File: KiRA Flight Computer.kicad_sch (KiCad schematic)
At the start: 44 parts, among them J1 Conn_01x04_Pin, J2 USB_C_Receptacle_USB2.0_14P, SW1 SW_Push, SW2 SW_SPDT, U1 ICM-426788P, U2 STM32F407VGTx, U3 MMC5883MA, U4 DPS368, U6 Wio-SX1262, U7 USBLC6-2P6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

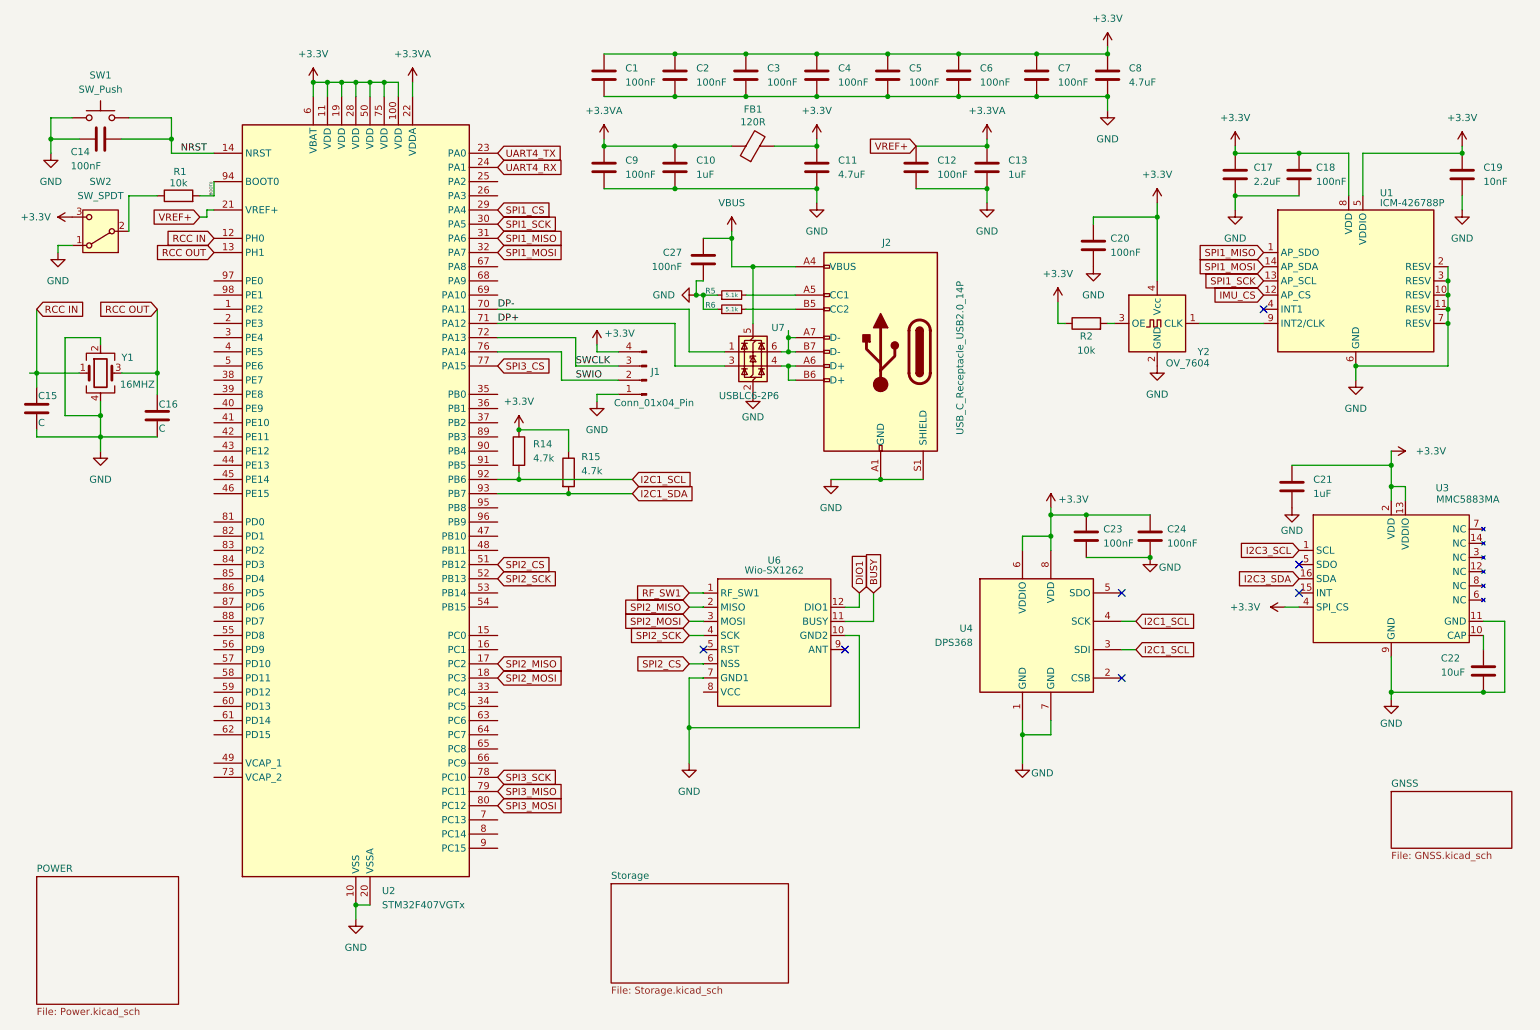
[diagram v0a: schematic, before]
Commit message: add sd card reader
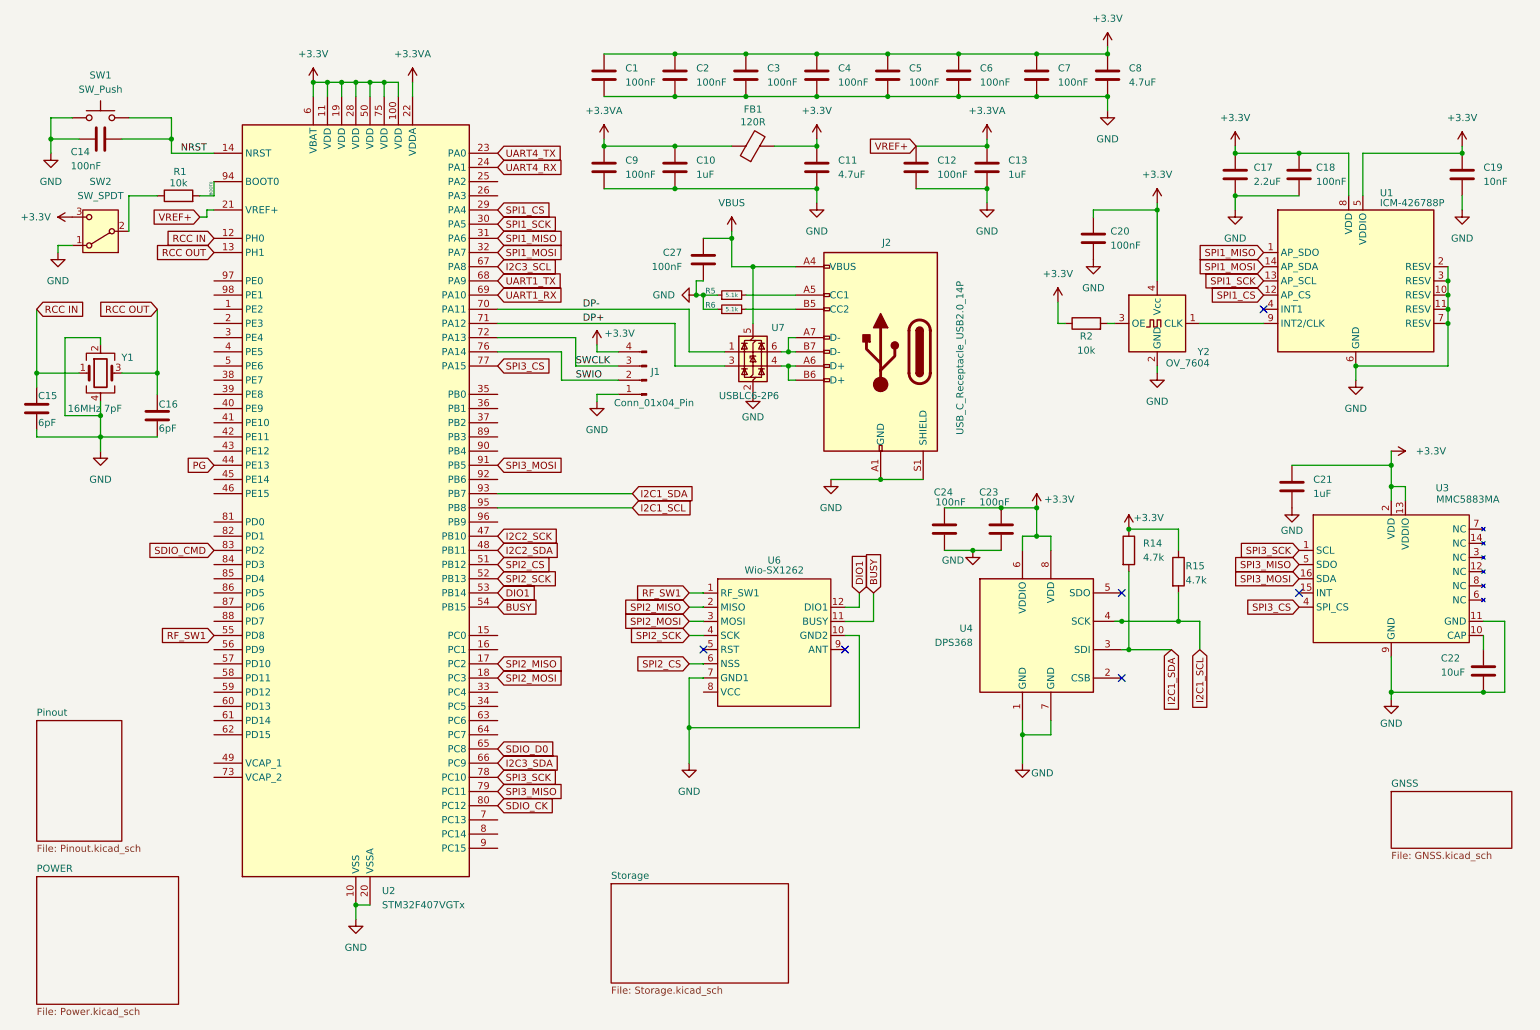
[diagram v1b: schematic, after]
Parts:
- C15, C16: value C -> 6pF
- Y1: value 16MHZ -> 16MHz 7pF
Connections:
- net IMU_CS is gone; now on net SPI1_CS: U1.12 (AP_CS)
- net +3.3V: no longer U3.4 (SPI_CS)
- net BUSY: now also U2.54 (PB15)
- net DIO1: now also U2.53 (PB14)
- net I2C1_SCL: now also R15.2, U2.95 (PB8); no longer R14.2, U2.92 (PB6), U4.3 (SDI)
- net I2C1_SDA: now also R14.2, U4.3 (SDI); no longer R15.2
- net I2C3_SCL: now also U2.67 (PA8); no longer U3.1 (SCL)
- net I2C3_SDA: now also U2.66 (PC9); no longer U3.16 (SDA)
- net RF_SW1: now also U2.55 (PD8)
- net SPI3_CS: now also U3.4 (SPI_CS)
- net SPI3_MISO: now also U3.5 (SDO)
- net SPI3_MOSI: now also U2.91 (PB5), U3.16 (SDA); no longer U2.80 (PC12)
- net SPI3_SCK: now also U3.1 (SCL)
- net PG: now reaches U2.44 (PE13)
- net I2C2_SCK: now reaches U2.47 (PB10)
- net I2C2_SDA: now reaches U2.48 (PB11)
- net SDIO_D0: now reaches U2.65 (PC8)
- net UART1_TX: now reaches U2.68 (PA9)
- net UART1_RX: now reaches U2.69 (PA10)
- net SDIO_CMD: now reaches U2.83 (PD2)
- new net SDIO_CK: U2.80 (PC12)
- no-connect marks 7 -> 6
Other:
- added sheet Pinout (Pinout.kicad_sch)
- moved on the sheet: C20, C23, C24, R14, R15

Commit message: "Update KiRA Flight Computer schematic and PCB files"
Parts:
- C1, C10, C11, C12, C13, C14, C15, C16, C17, C18, C2, C20, C21, C23, C24, C3, C4, C5, C6, C7, C8, C9: footprint (none) -> Capacitor_SMD:C_0603_1608Metric
- C19: footprint (none) -> Capacitor_SMD:C_0402_1005Metric
- C22: footprint (none) -> Capacitor_SMD:C_1206_3216Metric
- C27: footprint (none) -> Capacitor_SMD:C_0402_1005Metric_Pad0.74x0.62mm_HandSolder
- FB1: footprint (none) -> Inductor_SMD:L_1206_3216Metric
- J1: footprint (none) -> Connector_PinHeader_2.54mm:PinHeader_1x04_P2.54mm_Vertical
- J2: footprint (none) -> Connector_USB:USB_C_Receptacle_GCT_USB4105-xx-A_16P_TopMnt_Horizontal
- R1, R2: footprint (none) -> Resistor_SMD:R_0402_1005Metric
- R14, R15, R5, R6: footprint (none) -> Resistor_SMD:R_0603_1608Metric
- SW1: footprint (none) -> Button_Switch_SMD:SW_Push_1P1T_NO_CK_PTS125Sx43PSMTR
- SW2: footprint (none) -> Button_Switch_SMD:SW_SPDT_CK_JS102011SAQN
- U6: footprint ProLib_pcs_2024-10-14:Module:MODULE12P-1.27-11X11.6MM -> dep:WIO SX1262
- Y1: footprint (none) -> Crystal:Crystal_SMD_3225-4Pin_3.2x2.5mm
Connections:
- net +3.3V: now also U6.8 (VCC)
- net DP+: now also U7.1 (I/O1); no longer U7.3 (I/O2)
- net DP-: now also U7.3 (I/O2); no longer U7.1 (I/O1)
- net at J2.A6 (D+), J2.B6 (D+): now also U7.6 (I/O1); no longer U7.4 (I/O2)
- net at J2.A7 (D-), J2.B7 (D-): now also U7.4 (I/O2); no longer U7.6 (I/O1)
- net UART2_TX: now reaches U2.25 (PA2)
- net UART2_RX: now reaches U2.26 (PA3)
- net BUZZER: now reaches U2.56 (PD9)
- net MPU_CLK: now reaches U1.9 (INT2/CLK), Y2.1 (CLK)
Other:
- moved on the sheet: R5, R6, U7

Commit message: Update PCB
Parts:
- SW1: footprint Button_Switch_SMD:SW_Push_1P1T_NO_CK_PTS125Sx43PSMTR -> Button_Switch_SMD:SW_Push_1P1T_NO_CK_KSC6xxJ
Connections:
- net +3.3V: now also J1.1 (Pin_1); no longer J1.4 (Pin_4)
- net GND: now also J1.4 (Pin_4); no longer J1.1 (Pin_1)
- net SWCLK: now also J1.2 (Pin_2); no longer J1.3 (Pin_3)
- net SWIO: now also J1.3 (Pin_3); no longer J1.2 (Pin_2)
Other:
- moved on the sheet: J1
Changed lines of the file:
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@@
 	(paper "A4")
 	(junction
-		(at 135.89 63.5)
+		(at 217.17 48.26)
 		(diameter 0)
 		(color 0 0 0 0)
 	)
 	(junction
-		(at 217.17 48.26)
+		(at 135.89 63.5)
 		(diameter 0)
 		(color 0 0 0 0)
@@
 	)
 	(junction
+		(at 146.05 63.5)
+		(diameter 0)
+		(color 0 0 0 0)
+	)
+	(junction
 		(at 143.51 27.94)
 		(diameter 0)
@@
 	)
 	(junction
-		(at 134.62 63.5)
-		(diameter 0)
-		(color 0 0 0 0)
-	)
-	(junction
 		(at 16.51 77.47)
 		(diameter 0)
@@
 	)
 	(junction
-		(at 142.24 58.42)
-		(diameter 0)
-		(color 0 0 0 0)
-	)
-	(junction
 		(at 212.09 105.41)
 		(diameter 0)
@@
 	(wire
 		(pts
-			(xy 142.24 81.28) (xy 144.78 81.28)
-		)
-		(stroke
-			(width 0)
-			(type default)
-		)
-	)
-	(wire
-		(pts
 			(xy 156.21 20.32) (xy 168.91 20.32)
 		)
@@
 	(wire
 		(pts
-			(xy 135.89 66.04) (xy 135.89 63.5)
+			(xy 146.05 66.04) (xy 146.05 63.5)
 		)
 		(stroke
@@
 	(wire
 		(pts
-			(xy 146.05 66.04) (xy 135.89 66.04)
-		)
-		(stroke
-			(width 0)
-			(type default)
-		)
-	)
-	(wire
-		(pts
 			(xy 195.58 101.6) (xy 195.58 106.68)
 		)
@@
 	(wire
 		(pts
-			(xy 134.62 63.5) (xy 135.89 63.5)
-		)
-		(stroke
-			(width 0)
-			(type default)
-		)
-	)
-	(wire
-		(pts
 			(xy 259.08 128.27) (xy 259.08 134.62)
 		)
@@
 	(wire
 		(pts
+			(xy 135.89 63.5) (xy 146.05 63.5)
+		)
+		(stroke
+			(width 0)
+			(type default)
+		)
+	)
+	(wire
+		(pts
 			(xy 78.74 25.4) (xy 78.74 27.94)
 		)
@@
 	(wire
 		(pts
-			(xy 135.89 60.96) (xy 134.62 60.96)
-		)
-		(stroke
-			(width 0)
-			(type default)
-		)
-	)
-	(wire
-		(pts
-			(xy 142.24 58.42) (xy 152.4 58.42)
-		)
-		(stroke
-			(width 0)
-			(type default)
-		)
-	)
-	(wire
-		(pts
 			(xy 99.06 68.58) (xy 130.81 68.58)
 		)
@@
 	(wire
 		(pts
-			(xy 140.97 58.42) (xy 142.24 58.42)
+			(xy 140.97 58.42) (xy 152.4 58.42)
 		)
 		(stroke
@@
 	(wire
 		(pts
-			(xy 193.04 109.22) (xy 193.04 106.68)
+			(xy 135.89 63.5) (xy 134.62 63.5)
 		)
 		(stroke
@@
 	(wire
 		(pts
-			(xy 135.89 132.08) (xy 133.35 132.08)
+			(xy 193.04 109.22) (xy 193.04 106.68)
 		)
 		(stroke
@@
 	(wire
 		(pts
-			(xy 19.05 35.56) (xy 19.05 38.1)
+			(xy 135.89 132.08) (xy 133.35 132.08)
 		)
 		(stroke
@@
 	(wire
 		(pts
-			(xy 21.59 71.12) (xy 21.59 85.09)
+			(xy 19.05 35.56) (xy 19.05 38.1)
 		)
 		(stroke
@@
 	(wire
 		(pts
-			(xy 130.81 20.32) (xy 143.51 20.32)
+			(xy 21.59 71.12) (xy 21.59 85.09)
 		)
 		(stroke
@@
 	(wire
 		(pts
-			(xy 38.1 77.47) (xy 31.75 77.47)
+			(xy 130.81 20.32) (xy 143.51 20.32)
 		)
 		(stroke
@@
 	(wire
 		(pts
-			(xy 156.21 35.56) (xy 156.21 36.83)
+			(xy 38.1 77.47) (xy 31.75 77.47)
 		)
 		(stroke
@@
 	(wire
 		(pts
-			(xy 219.71 127) (xy 212.09 127)
+			(xy 156.21 35.56) (xy 156.21 36.83)
 		)
 		(stroke
@@
 	(wire
 		(pts
-			(xy 135.89 63.5) (xy 146.05 63.5)
+			(xy 219.71 127) (xy 212.09 127)
 		)
 		(stroke
@@
 	(wire
 		(pts
-			(xy 142.24 58.42) (xy 142.24 68.58)
-		)
-		(stroke
-			(width 0)
-			(type default)
-		)
-	)
-	(wire
-		(pts
 			(xy 133.35 66.04) (xy 133.35 76.2)
 		)
@@
 	(wire
 		(pts
-			(xy 134.62 60.96) (xy 134.62 63.5)
+			(xy 135.89 60.96) (xy 135.89 63.5)
 		)
 		(stroke
@@
 	(wire
 		(pts
+			(xy 142.24 67.31) (xy 142.24 68.58)
+		)
+		(stroke
+			(width 0)
+			(type default)
+		)
+	)
+	(wire
+		(pts
 			(xy 71.12 25.4) (xy 71.12 27.94)
 		)
@@
 			)
 		)
-		(property "Footprint" "Button_Switch_SMD:SW_Push_1P1T_NO_CK_PTS125Sx43PSMTR"
+		(property "Footprint" "Button_Switch_SMD:SW_Push_1P1T_NO_CK_KSC6xxJ"
 			(at 27.94 26.67 0)
 			(effects
@@
 	(symbol
 		(lib_id "power:GND")
-		(at 144.78 81.28 0)
+		(at 142.24 81.28 0)
 		(unit 1)
 		(exclude_from_sim no)
@@
 		(dnp no)
 		(property "Reference" "#PWR042"
-			(at 144.78 87.63 0)
+			(at 142.24 87.63 0)
 			(effects
 				(font
@@
 		)
 		(property "Value" "GND"
-			(at 144.78 85.344 0)
+			(at 142.24 85.344 0)
 			(effects
 				(font
@@
 		)
 		(property "Footprint" ""
-			(at 144.78 81.28 0)
+			(at 142.24 81.28 0)
 			(effects
 				(font
@@
 		)
 		(property "Datasheet" ""
-			(at 144.78 81.28 0)
+			(at 142.24 81.28 0)
 			(effects
 				(font
@@
 		)
 		(property "Description" "Power symbol creates a global label with name \"GND\" , ground"
-			(at 144.78 81.28 0)
+			(at 142.24 81.28 0)
 			(effects
 				(font
@@
 	(symbol
 		(lib_id "Connector:Conn_01x04_Pin")
-		(at 125.73 78.74 180)
+		(at 125.73 76.2 0)
+		(mirror y)
 		(unit 1)
 		(exclude_from_sim no)
@@
 		(dnp no)
 		(property "Reference" "J1"
-			(at 126.492 77.216 0)
+			(at 126.492 77.724 0)
 			(effects
 				(font
@@
 		)
 		(property "Value" "Conn_01x04_Pin"
-			(at 119.888 82.804 0)
+			(at 119.888 85.344 0)
 			(effects
 				(font
@@
 		)
 		(property "Footprint" "Connector_PinHeader_2.54mm:PinHeader_1x04_P2.54mm_Vertical"
-			(at 125.73 78.74 0)
+			(at 125.73 76.2 0)
 			(effects
 				(font
@@
 		)
 		(property "Datasheet" "~"
-			(at 125.73 78.74 0)
+			(at 125.73 76.2 0)
 			(effects
 				(font
@@
 		)
 		(property "Description" "Generic connector, single row, 01x04, script generated"
-			(at 125.73 78.74 0)
+			(at 125.73 76.2 0)
 			(effects
 				(font
@@
 	)
 	(symbol
+		(lib_id "power:VBUS")
+		(at 142.24 67.31 90)
+		(unit 1)
+		(exclude_from_sim no)
+		(in_bom yes)
+		(on_board yes)
+		(dnp no)
+		(fields_autoplaced yes)
+		(property "Reference" "#PWR073"
+			(at 146.05 67.31 0)
+			(effects
+				(font
+					(size 1.27 1.27)
+				)
+				(hide yes)
+			)
+		)
+		(property "Value" "VBUS"
+			(at 138.43 67.3099 90)
+			(effects
+				(font
+					(size 1.27 1.27)
+				)
+				(justify left)
+			)
+		)
+		(property "Footprint" ""
+			(at 142.24 67.31 0)
+			(effects
+				(font
+					(size 1.27 1.27)
+				)
+				(hide yes)
+			)
+		)
+		(property "Datasheet" ""
+			(at 142.24 67.31 0)
+			(effects
+				(font
+					(size 1.27 1.27)
+				)
+				(hide yes)
+			)
+		)
+		(property "Description" "Power symbol creates a global label with name \"VBUS\""
+			(at 142.24 67.31 0)
+			(effects
+				(font
+					(size 1.27 1.27)
+				)
+				(hide yes)
+			)
+		)
+		(pin "1"
+		)
+		(instances
+			(project "KiRA Flight Computer"
+				(path "/aff8106b-a9b7-4e48-85ad-25b2eb3ce379"
+					(reference "#PWR073")
+					(unit 1)
+				)
+			)
+		)
+	)
+	(symbol
 		(lib_id "power:GND")
 		(at 158.75 96.52 0)
@@
 		(on_board yes)
 		(dnp no)
-		(fields_autoplaced yes)
 		(property "Reference" "SW2"
 			(at 27.94 43.18 0)
@@
 					(reference "SW2")
 					(unit 1)
+				)
+				(path "/aff8106b-a9b7-4e48-85ad-25b2eb3ce379/ba160f04-df44-4adc-a5a3-9beb293319f2"
+					(reference "SW2")
+					(unit 1)

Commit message: Update PCB
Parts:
- C19: footprint Capacitor_SMD:C_0402_1005Metric -> Capacitor_SMD:C_0603_1608Metric
- R1, R2: footprint Resistor_SMD:R_0402_1005Metric -> Resistor_SMD:R_0603_1608Metric
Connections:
- net SPI1_CS: now also U6.6 (NSS); no longer U1.12 (AP_CS)
- net SPI1_MISO: now also U6.2 (MISO); no longer U1.1 (AP_SDO)
- net SPI1_MOSI: now also U6.3 (MOSI); no longer U1.14 (AP_SDA)
- net SPI1_SCK: now also U6.4 (SCK); no longer U1.13 (AP_SCL)
- net SPI2_CS: now also U1.12 (AP_CS); no longer U6.6 (NSS)
- net SPI2_MISO: now also U1.1 (AP_SDO); no longer U6.2 (MISO)
- net SPI2_MOSI: now also U1.14 (AP_SDA); no longer U6.3 (MOSI)
- net SPI2_SCK: now also U1.13 (AP_SCL); no longer U6.4 (SCK)
- net UART1_RX: no longer names the net of U2.69 (PA10)
- net UART1_TX: no longer names the net of U2.68 (PA9)
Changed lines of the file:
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@@
 	(global_label "SPI1_MOSI"
 		(shape input)
-		(at 236.22 58.42 180)
+		(at 133.35 121.92 180)
 		(fields_autoplaced yes)
 		(effects
@@
 		)
 		(property "Intersheetrefs" "${INTERSHEET_REFS}"
-			(at 223.3772 58.42 0)
+			(at 120.5072 121.92 0)
 			(effects
 				(font
@@
 	(global_label "SPI2_SCK"
 		(shape input)
-		(at 133.35 124.46 180)
+		(at 236.22 60.96 180)
 		(fields_autoplaced yes)
 		(effects
@@
 		)
 		(property "Intersheetrefs" "${INTERSHEET_REFS}"
-			(at 121.3539 124.46 0)
+			(at 224.2239 60.96 0)
 			(effects
 				(font
@@
 	(global_label "SPI1_MISO"
 		(shape input)
-		(at 236.22 55.88 180)
+		(at 133.35 119.38 180)
 		(fields_autoplaced yes)
 		(effects
@@
 		)
 		(property "Intersheetrefs" "${INTERSHEET_REFS}"
-			(at 223.3772 55.88 0)
+			(at 120.5072 119.38 0)
 			(effects
 				(font
@@
 	(global_label "SPI2_CS"
 		(shape input)
-		(at 133.35 129.54 180)
+		(at 236.22 63.5 180)
 		(fields_autoplaced yes)
 		(effects
@@
 		)
 		(property "Intersheetrefs" "${INTERSHEET_REFS}"
-			(at 122.6239 129.54 0)
+			(at 225.4939 63.5 0)
 			(effects
 				(font
@@
 		)
 	)
-	(global_label "UART1_TX"
-		(shape input)
-		(at 99.06 60.96 0)
-		(fields_autoplaced yes)
-		(effects
-			(font
-				(size 1.27 1.27)
-			)
-			(justify left)
-		)
-		(property "Intersheetrefs" "${INTERSHEET_REFS}"
-			(at 111.0561 60.96 0)
-			(effects
-				(font
-					(size 1.27 1.27)
-				)
-				(justify left)
-				(hide yes)
-			)
-		)
-	)
 	(global_label "I2C2_SDA"
 		(shape input)
@@
 		)
 	)
-	(global_label "UART1_RX"
-		(shape input)
-		(at 99.06 63.5 0)
-		(fields_autoplaced yes)
-		(effects
-			(font
-				(size 1.27 1.27)
-			)
-			(justify left)
-		)
-		(property "Intersheetrefs" "${INTERSHEET_REFS}"
-			(at 111.3585 63.5 0)
-			(effects
-				(font
-					(size 1.27 1.27)
-				)
-				(justify left)
-				(hide yes)
-			)
-		)
-	)
 	(global_label "UART2_TX"
 		(shape input)
@@
 	(global_label "SPI2_MISO"
 		(shape input)
-		(at 133.35 119.38 180)
+		(at 236.22 55.88 180)
 		(fields_autoplaced yes)
 		(effects
@@
 		)
 		(property "Intersheetrefs" "${INTERSHEET_REFS}"
-			(at 120.5072 119.38 0)
+			(at 223.3772 55.88 0)
 			(effects
 				(font
@@
 	(global_label "SPI2_MOSI"
 		(shape input)
-		(at 133.35 121.92 180)
+		(at 236.22 58.42 180)
 		(fields_autoplaced yes)
 		(effects
@@
 		)
 		(property "Intersheetrefs" "${INTERSHEET_REFS}"
-			(at 120.5072 121.92 0)
+			(at 223.3772 58.42 0)
 			(effects
 				(font
@@
 	(global_label "SPI1_SCK"
 		(shape input)
-		(at 236.22 60.96 180)
+		(at 133.35 124.46 180)
 		(fields_autoplaced yes)
 		(effects
@@
 		)
 		(property "Intersheetrefs" "${INTERSHEET_REFS}"
-			(at 224.2239 60.96 0)
+			(at 121.3539 124.46 0)
 			(effects
 				(font
@@
 	(global_label "SPI1_CS"
 		(shape input)
-		(at 236.22 63.5 180)
+		(at 133.35 129.54 180)
 		(fields_autoplaced yes)
 		(effects
@@
 		)
 		(property "Intersheetrefs" "${INTERSHEET_REFS}"
-			(at 225.4939 63.5 0)
+			(at 122.6239 129.54 0)
 			(effects
 				(font
@@
 			)
 		)
-		(property "Footprint" "Capacitor_SMD:C_0402_1005Metric"
+		(property "Footprint" "Capacitor_SMD:C_0603_1608Metric"
 			(at 272.7452 45.72 0)
 			(effects
@@
 			)
 		)
-		(property "Footprint" "Resistor_SMD:R_0402_1005Metric"
+		(property "Footprint" "Resistor_SMD:R_0603_1608Metric"
 			(at 204.47 70.358 90)
 			(effects
@@
 			)
 		)
-		(property "Footprint" "Resistor_SMD:R_0402_1005Metric"
+		(property "Footprint" "Resistor_SMD:R_0603_1608Metric"
 			(at 41.91 47.498 90)
 			(effects

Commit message: Update PCB
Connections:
- net BUSY: now also U2.43 (PE12); no longer U2.54 (PB15)
- net DIO1: now also U2.42 (PE11); no longer U2.53 (PB14)
- net RF_SW1: now also U2.41 (PE10); no longer U2.55 (PD8)
- net PWM3: now reaches U2.4 (PE5)
- net PWM4: now reaches U2.5 (PE6)
- net PWM2: now reaches U2.59 (PD12)
- net PWM1: now reaches U2.60 (PD13)
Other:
- moved on the sheet: C15, C16, Y1

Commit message: questionable changes
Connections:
- net BUZZER: now also U2.88 (PD7); no longer U2.56 (PD9)
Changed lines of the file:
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@@
 	(global_label "BUZZER"
 		(shape input)
-		(at 48.26 127 180)
+		(at 48.26 121.92 180)
 		(fields_autoplaced yes)
 		(effects
@@
 		)
 		(property "Intersheetrefs" "${INTERSHEET_REFS}"
-			(at 37.8363 127 0)
+			(at 37.8363 121.92 0)
 			(effects
 				(font

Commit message: PCB Update
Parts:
- removed C17: 2.2uF, Capacitor_SMD:C_0603_1608Metric, symbol Device:C
- removed C18, C20: 100nF, Capacitor_SMD:C_0603_1608Metric, symbol Device:C
- removed C19: 10nF, Capacitor_SMD:C_0603_1608Metric, symbol Device:C
- removed R2: 10k, Resistor_SMD:R_0603_1608Metric, symbol Device:R
- removed U1: ICM-426788P, Package_LGA:Bosch_LGA-14_3x2.5mm_P0.5mm, symbol Sensor_Motion:BMI160
- removed Y2: OV_7604, Oscillator:Oscillator_SMD_SeikoEpson_SG3030CM, symbol Oscillator:SG-3030CM
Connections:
- net +3.3V: no longer C7.1
- net BUSY: now also U2.53 (PB14); no longer U2.43 (PE12)
- net DIO1: now also U2.54 (PB15); no longer U2.42 (PE11)
- net RF_SW1: now also U2.57 (PD10); no longer U2.41 (PE10)
- net SPI1_CS: now also U3.4 (SPI_CS); no longer U6.6 (NSS)
- net SPI1_MISO: now also U3.5 (SDO); no longer U6.2 (MISO)
- net SPI1_MOSI: now also U3.16 (SDA); no longer U6.3 (MOSI)
- net SPI1_SCK: now also U3.1 (SCL); no longer U6.4 (SCK)
- net SPI3_CS: now also U6.6 (NSS); no longer U3.4 (SPI_CS)
- net SPI3_MISO: now also U6.2 (MISO); no longer U3.5 (SDO)
- net SPI3_MOSI: now also U6.3 (MOSI); no longer U3.16 (SDA)
- net SPI3_SCK: now also U6.4 (SCK); no longer U3.1 (SCL)
- net UART3_TX: now reaches U2.55 (PD8)
- net UART3_RX: now reaches U2.56 (PD9)
- net RX: now reaches U2.63 (PC6)
- net TX: now reaches U2.64 (PC7)
- net PY2: now reaches U2.98 (PE1)
- net PG: no longer names the net of U2.44 (PE13)
- new net PY1: U2.43 (PE12)
- no-connect marks 6 -> 5
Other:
- added sheet IMUs (IMUS.kicad_sch)
